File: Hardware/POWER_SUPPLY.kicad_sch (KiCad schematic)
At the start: 47 parts, among them U2 LM5164DDAR, U3 MP1605GTF-Z, U5 JW5026, U6 MP1605GTF-Z, U7 LP5907MFX-3.3/NOPB, U8 REF3030AIDBZR

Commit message: 拉线
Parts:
- added R131: 0R,1%, Resistor_SMD:R_0805_2012Metric, symbol HPM6280Foc:0805W8F0000T5E
- U4: footprint Connector_AMASS:AMASS_XT30UPB-F_1x02_P5.0mm_Vertical -> Connector_AMASS:AMASS_XT60-M_1x02_P7.20mm_Vertical
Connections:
- net +3V3 is gone; now on net +3.3V: R10.1
- net GND: now also R131.2
- net GNDPWR: now also R131.1
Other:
- moved on the sheet: L1, L3

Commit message: 拉线
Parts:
- added F3: JFC2410-1100TS, Library:JFC2410, symbol HPM6280Foc:JFC2410-1100TS
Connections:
- net VBUS: now also F3.1; no longer C28.1, C47.2, U2.2 (VIN), U2.3 (EN/UVLO)
- new net VBUS_F: C28.1, C47.2, F3.2, U2.2 (VIN), U2.3 (EN/UVLO)

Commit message: 修存档拉线
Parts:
- renumbered C29 to C10, C30 to C11, C31 to C12, C32 to C13, C33 to C14, C34 to C15, C35 to C16, C36 to C17, C37 to C18, C38 to C19, C39 to C20, C40 to C21, C41 to C22, C42 to C23, C43 to C24, C44 to C25, C45 to C26, C46 to C27, C47 to C28, C28 to C9, D3 to D11, D4 to D12, D5 to D13, F3 to F1, FB2 to FB1, FB3 to FB2, R10 to R14, R11 to R15, R12 to R16, R13 to R17, R14 to R18, R15 to R19, R16 to R20, R17 to R22, R18 to R23, R19 to R24, R20 to R25, R131 to R26, U8 to U10, U2 to U4, U3 to U5, U4 to U6, U5 to U7, U6 to U8, U7 to U9
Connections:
- net GND: no longer C12.2, C13.2, C9.2, R16.2, R18.2, U4.1 (GND), U4.9 (EP)
- net GNDPWR: now also C12.2, C13.2, C9.2, R16.2, R18.2, U4.1 (GND), U4.9 (EP)
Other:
- moved on the sheet: D11, R26, U6

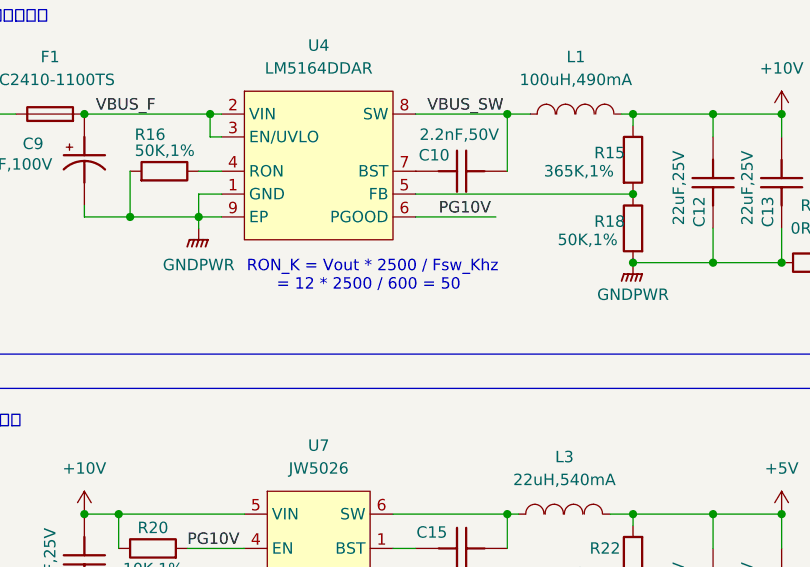
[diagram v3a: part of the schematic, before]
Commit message: 拉线，增加刹车电阻
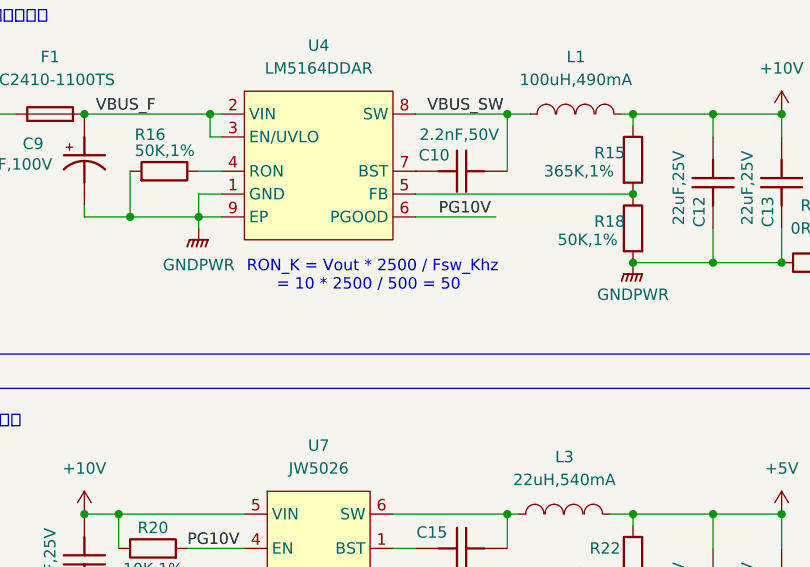
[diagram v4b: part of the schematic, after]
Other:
- note added: "RON_K = Vout * 2500 / Fsw_Khz = 10 * 2500 / 500 = 50"
- note removed: "RON_K = Vout * 2500 / Fsw_Khz = 12 * 2500 / 600 = 50"
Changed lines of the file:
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@@
 		)
 	)
-	(text "RON_K = Vout * 2500 / Fsw_Khz\n      = 12 * 2500 / 600 = 50"
+	(text "RON_K = Vout * 2500 / Fsw_Khz\n      = 10 * 2500 / 500 = 50"
 		(exclude_from_sim yes)
 		(at 113.284 57.404 0)

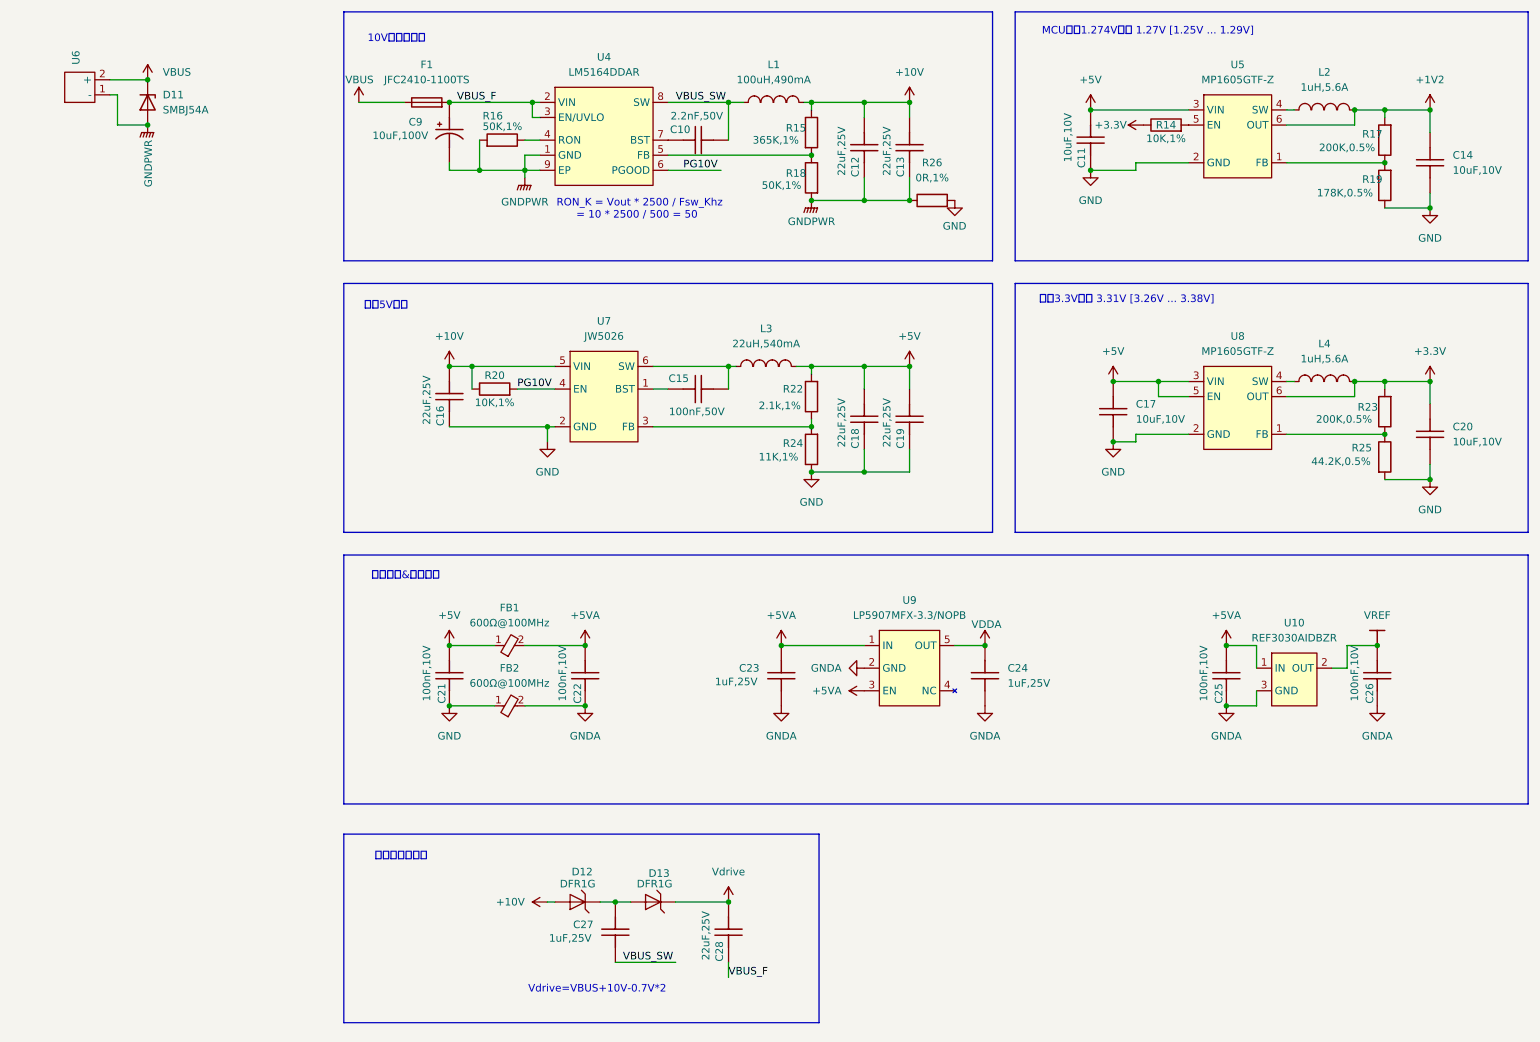
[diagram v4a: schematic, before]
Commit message: 拉线，删除电荷泵，修改10Vdcdc斜坡补偿
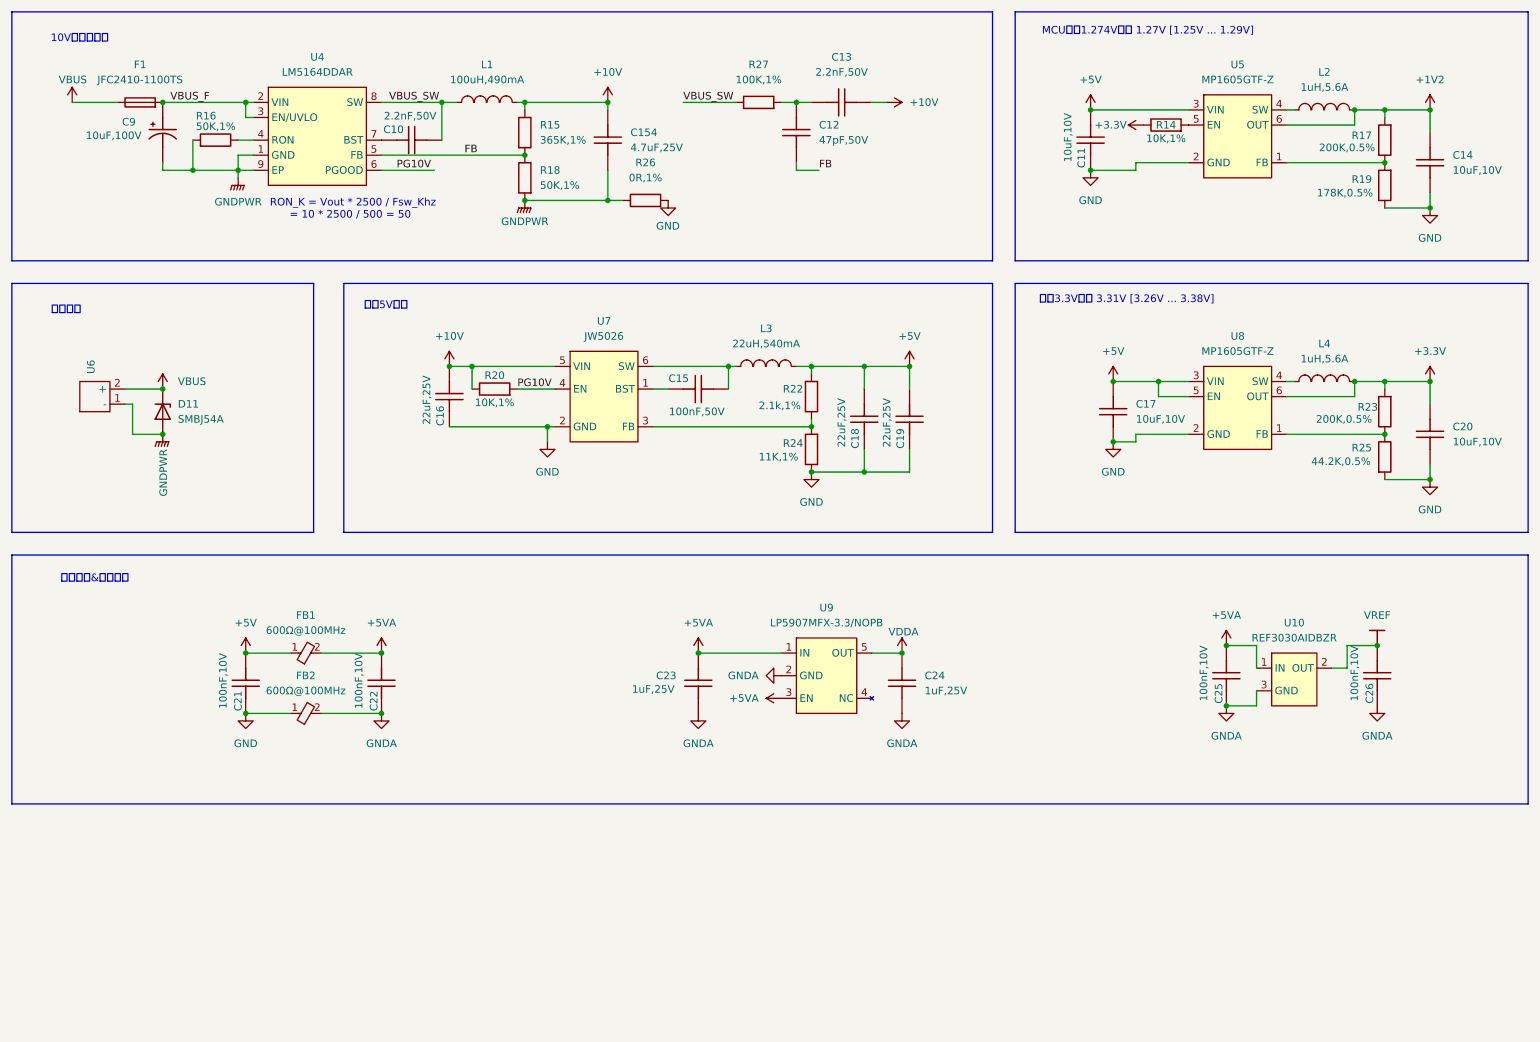
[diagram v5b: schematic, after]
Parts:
- removed C12, C13, C28: 22uF,25V, Capacitor_SMD:C_0805_2012Metric, symbol HPM6280Foc:CL21A226MAYNNNE
- removed C27: 1uF,25V, Capacitor_SMD:C_0402_1005Metric, symbol HPM6280Foc:CL05A105KA5NQNC
- removed D12, D13: DFR1G, Diode_SMD:D_SOD-123, symbol HPM6280Foc:DFR1G
- added C12: 47pF,50V, Capacitor_SMD:C_0402_1005Metric, symbol HPM6280Foc:CC0402JRNPO9BN470
- added C13: 2.2nF,50V, Capacitor_SMD:C_0402_1005Metric, symbol HPM6280Foc:0402B222K500NT
- added C154: 4.7uF,25V, Capacitor_SMD:C_0805_2012Metric, symbol HPM6280Foc:CL21A475KAQNNNE
- added R27: 100K,1%, Resistor_SMD:R_0402_1005Metric, symbol HPM6280Foc:RC0402FR-0710KL
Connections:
- net +10V: now also C13.2, C154.1
- net GNDPWR: now also C154.2
- net VBUS_SW: now also R27.1
- net FB: now reaches R15.2, R18.1, U4.5 (FB)
- net FB: now also C12.2
- new net: C12.1, C13.1, R27.2
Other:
- note added: "输入插座"
- note removed: "Vdrive=VBUS+10V-0.7V*2"
- note removed: "高侧驱动电荷泵"
- moved on the sheet: C10, C21, C22, C23, C24, C9, D11, F1, FB1, FB2, L1, R15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

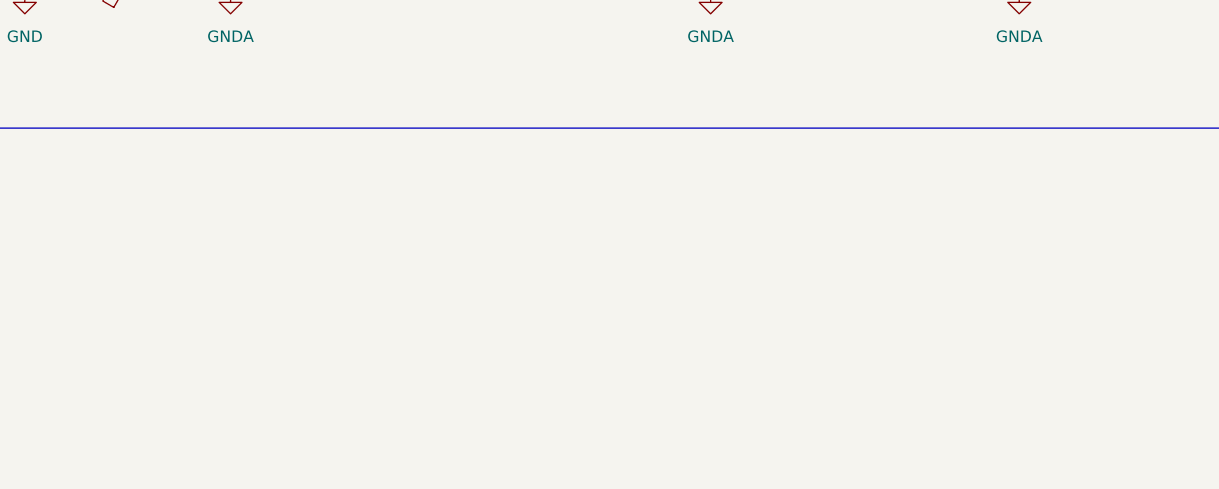
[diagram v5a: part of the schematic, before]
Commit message: 添加母线电压测量
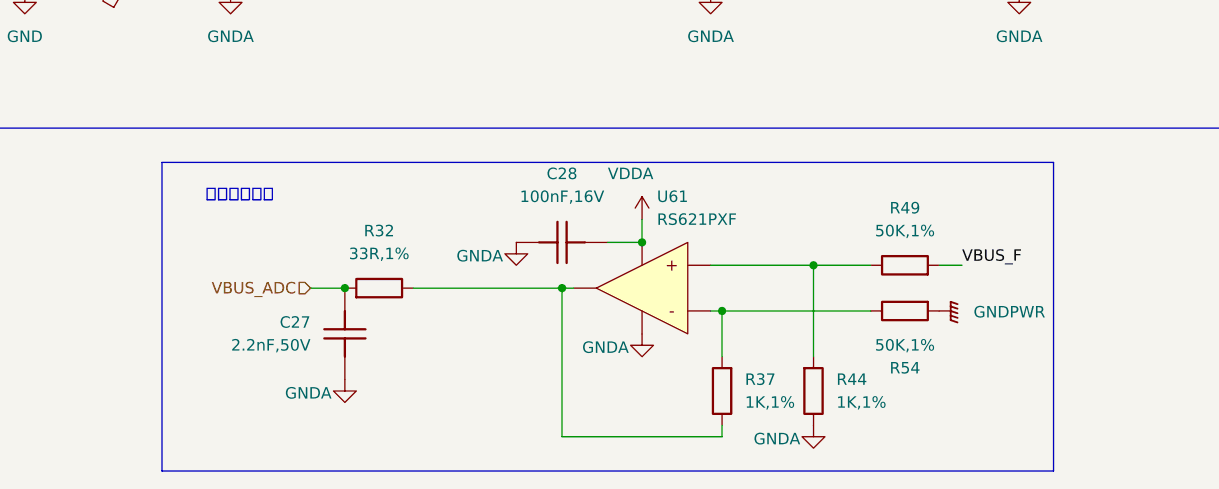
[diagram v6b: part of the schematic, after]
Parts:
- added C27: 2.2nF,50V, Capacitor_SMD:C_0402_1005Metric, symbol HPM6280Foc:0402B222K500NT
- added C28: 100nF,16V, Capacitor_SMD:C_0402_1005Metric, symbol HPM6280Foc:CC0402KRX7R7BB104
- added R32: 33R,1%, Resistor_SMD:R_0402_1005Metric, symbol HPM6280Foc:0402WGF330JTCE
- added R37, R44: 1K,1%, Resistor_SMD:R_0402_1005Metric, symbol HPM6280Foc:0402WGF1001TCE
- added R49, R54: 50K,1%, Resistor_SMD:R_0402_1005Metric, symbol HPM6280Foc:RTT025002FTH
- added U61: RS621PXF, Package_TO_SOT_SMD:SOT-23-5, symbol HPM6280Foc:RS621PXF
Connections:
- net GNDA: now also C27.2, C28.2, R44.1, U61.2 (V-)
- net GNDPWR: now also R54.2
- net VBUS_F: now also R49.2
- net VDDA: now also C28.1, U61.5 (V+)
- new net: R32.1, R37.1, U61.1 (OUT)
- new net: R44.2, R49.1, U61.3 (+IN)
- new net: R37.2, R54.1, U61.4 (-IN)
- new net VBUS_ADC: C27.1, R32.2
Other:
- note added: "母线电压采集"

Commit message: 修饰，第一次打板
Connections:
- net +5V: now also R24.2; no longer R22.2
- net GND: now also R22.1; no longer R24.1
- new net: R22.2, R24.1, U7.3 (FB)
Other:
- moved on the sheet: R22, R24

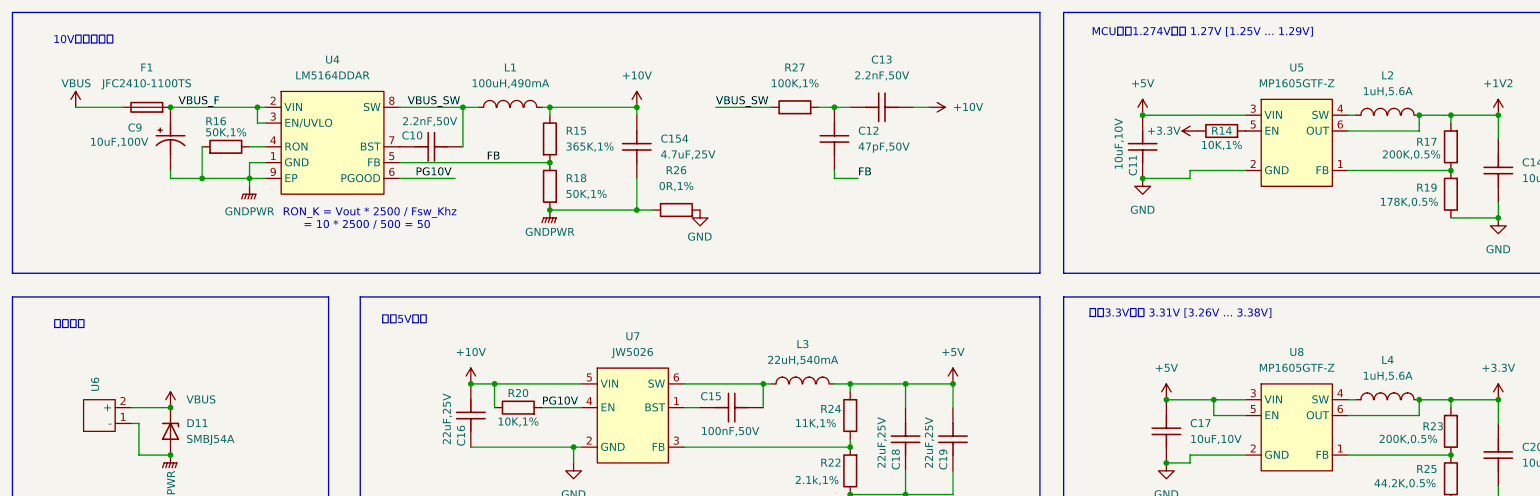
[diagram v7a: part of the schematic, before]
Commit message: 修改PCB，上传py32抱闸驱动代码，上传HPM board
调整抱闸驱动栅极电阻
急停光耦增加上拉电阻和滤波电路
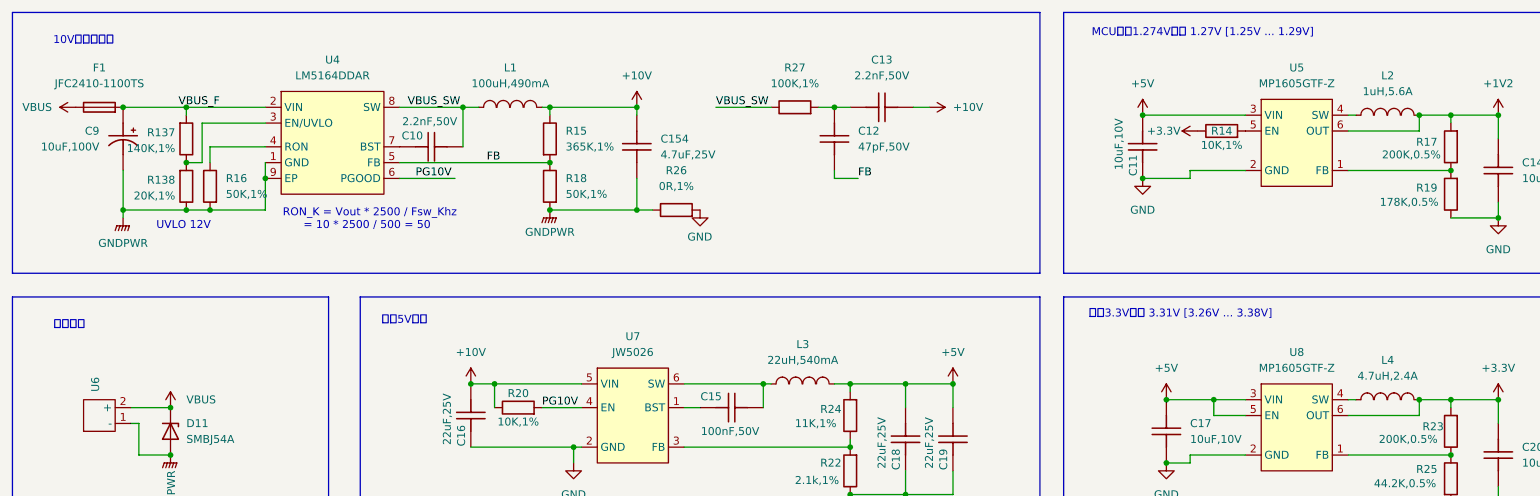
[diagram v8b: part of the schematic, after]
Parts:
- added R137: 140K,1%, Resistor_SMD:R_0402_1005Metric, symbol HPM6280Foc:0402WGF1403TCE
- added R138: 20K,1%, Resistor_SMD:R_0402_1005Metric, symbol HPM6280Foc:0402WGF2002TCE
- L4: value 1uH,5.6A -> 4.7uH,2.4A; symbol HPM6280Foc:FTC252012S1R0MBCA -> HPM6280Foc:FTC252012S4R7MBCA; 制造商 (none) -> Sumida(胜美达); 华秋编号 G6636520 -> G4665211; 立创编号 C5832370 -> C5832374
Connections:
- net GNDPWR: now also R138.1
- net VBUS_F: now also R137.2; no longer U4.3 (EN/UVLO)
- new net: R137.1, R138.2, U4.3 (EN/UVLO)
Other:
- note added: "UVLO 12V"
- moved on the sheet: C9, F1, R16
